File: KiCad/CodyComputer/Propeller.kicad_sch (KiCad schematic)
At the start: 25 parts, among them J1 Barrel_Jack, J2 Power LED, J3 PropPlug, J4 Video Out, J5 Audio Out, U1 74HC541, U2 LM2937ET-3.3, U3 P8X32A-D40, U4 24LC256, Y1 5MHz

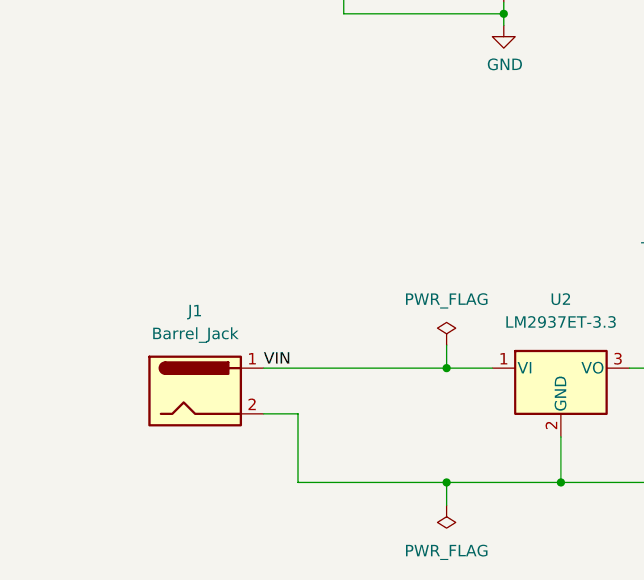
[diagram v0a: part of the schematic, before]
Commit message: Add debug power connector to schematic
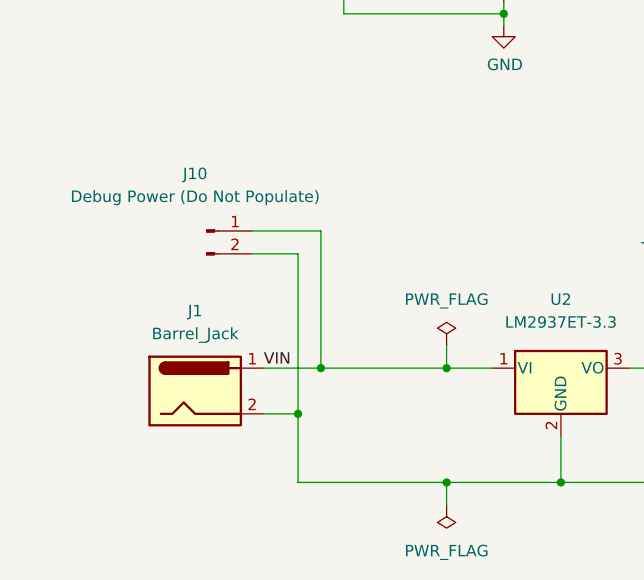
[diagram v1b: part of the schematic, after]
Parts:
- added J10: Debug Power (Do Not Populate), Connector_PinHeader_2.54mm:PinHeader_1x02_P2.54mm_Vertical, symbol Connector:Conn_01x02_Male
- U1: footprint Package_DIP:DIP-20_W7.62mm_Socket -> Package_DIP:DIP-20_W7.62mm_Socket_LongPads
- U3: footprint Package_DIP:DIP-40_W15.24mm_Socket -> Package_DIP:DIP-40_W15.24mm_Socket_LongPads
- U4: footprint Package_DIP:DIP-8_W7.62mm_Socket -> Package_DIP:DIP-8_W7.62mm_Socket_LongPads
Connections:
- net GND: now also J10.2 (Pin_2)
- net VIN: now also J10.1 (Pin_1)
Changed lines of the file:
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@@
   (title_block
     (title "Propeller, Bus Multiplexing, Video/Audio, Power")
-    (date "2023-04-18")
-    (rev "A")
+    (date "2025-01-06")
+    (rev "B")
   )
   (junction (at 90.17 143.51) (diameter 0) (color 0 0 0 0)
@@
   (junction (at 72.39 91.44) (diameter 0) (color 0 0 0 0)
   )
+  (junction (at 52.07 130.81) (diameter 0) (color 0 0 0 0)
+  )
   (junction (at 100.33 69.85) (diameter 0) (color 0 0 0 0)
   )
@@
   (junction (at 210.82 139.7) (diameter 0) (color 0 0 0 0)
   )
+  (junction (at 49.53 135.89) (diameter 0) (color 0 0 0 0)
+  )
   (junction (at 148.59 40.64) (diameter 0) (color 0 0 0 0)
   )
@@
     (stroke (width 0) (type default) (color 0 0 0 0))
   )
+  (wire (pts (xy 44.45 115.57) (xy 52.07 115.57))
+    (stroke (width 0) (type default) (color 0 0 0 0))
+  )
   (wire (pts (xy 125.73 46.99) (xy 125.73 49.53))
     (stroke (width 0) (type default) (color 0 0 0 0))
@@
     (stroke (width 0) (type default) (color 0 0 0 0))
   )
-  (wire (pts (xy 45.72 130.81) (xy 66.04 130.81))
+  (wire (pts (xy 45.72 130.81) (xy 52.07 130.81))
     (stroke (width 0) (type default) (color 0 0 0 0))
   )
@@
     (stroke (width 0) (type default) (color 0 0 0 0))
   )
+  (wire (pts (xy 44.45 118.11) (xy 49.53 118.11))
+    (stroke (width 0) (type default) (color 0 0 0 0))
+  )
   (wire (pts (xy 102.87 72.39) (xy 130.81 72.39))
     (stroke (width 0) (type default) (color 0 0 0 0))
@@
     (stroke (width 0) (type default) (color 0 0 0 0))
   )
+  (wire (pts (xy 49.53 118.11) (xy 49.53 135.89))
+    (stroke (width 0) (type default) (color 0 0 0 0))
+  )
   (wire (pts (xy 85.09 72.39) (xy 102.87 72.39))
     (stroke (width 0) (type default) (color 0 0 0 0))
@@
     (stroke (width 0) (type default) (color 0 0 0 0))
   )
+  (wire (pts (xy 52.07 130.81) (xy 66.04 130.81))
+    (stroke (width 0) (type default) (color 0 0 0 0))
+  )
   (wire (pts (xy 184.15 134.62) (xy 166.37 134.62))
     (stroke (width 0) (type default) (color 0 0 0 0))
@@
   )
   (wire (pts (xy 200.66 144.78) (xy 200.66 146.05))
+    (stroke (width 0) (type default) (color 0 0 0 0))
+  )
+  (wire (pts (xy 52.07 115.57) (xy 52.07 130.81))
     (stroke (width 0) (type default) (color 0 0 0 0))
   )
@@
     (property "Reference" "U3" (id 0) (at 157.48 43.18 0))
     (property "Value" "P8X32A-D40" (id 1) (at 157.48 45.72 0))
-    (property "Footprint" "Package_DIP:DIP-40_W15.24mm_Socket" (id 2) (at 148.59 41.91 0)
+    (property "Footprint" "Package_DIP:DIP-40_W15.24mm_Socket_LongPads" (id 2) (at 148.59 41.91 0)
       (effects (font (size 1.27 1.27)) hide)
     )
@@
     (property "Reference" "U1" (id 0) (at 78.74 49.53 0))
     (property "Value" "74HC541" (id 1) (at 78.74 52.07 0))
-    (property "Footprint" "Package_DIP:DIP-20_W7.62mm_Socket" (id 2) (at 72.39 69.85 0)
+    (property "Footprint" "Package_DIP:DIP-20_W7.62mm_Socket_LongPads" (id 2) (at 72.39 69.85 0)
       (effects (font (size 1.27 1.27)) hide)
     )
@@
     (property "Reference" "U4" (id 0) (at 208.28 127 0))
     (property "Value" "24LC256" (id 1) (at 208.28 129.54 0))
-    (property "Footprint" "Package_DIP:DIP-8_W7.62mm_Socket" (id 2) (at 200.66 137.16 0)
+    (property "Footprint" "Package_DIP:DIP-8_W7.62mm_Socket_LongPads" (id 2) (at 200.66 137.16 0)
       (effects (font (size 1.27 1.27)) hide)
     )
@@
       (effects (font (size 1.27 1.27)) hide)
     )
+    (pin "1")
+    (pin "2")
+  )
+  (symbol (lib_id "Connector:Conn_01x02_Male") (at 39.37 115.57 0) (unit 1)
+    (in_bom yes) (on_board yes)
+    (property "Reference" "J10" (id 0) (at 38.1 109.22 0))
+    (property "Value" "Debug Power (Do Not Populate)" (id 1) (at 38.1 111.76 0))
+    (property "Footprint" "Connector_PinHeader_2.54mm:PinHeader_1x02_P2.54mm_Vertical" (id 2) (at 39.37 115.57 0)
+      (effects (font (size 1.27 1.27)) hide)
+    )
+    (property "Datasheet" "~" (id 3) (at 39.37 115.57 0)
+      (effects (font (size 1.27 1.27)) hide)
+    )
